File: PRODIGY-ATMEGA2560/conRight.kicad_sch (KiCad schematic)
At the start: 1 part, among them J2 DF40C-100DS-0.4V(51)

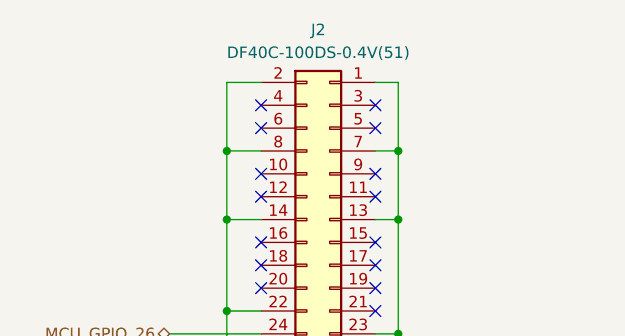
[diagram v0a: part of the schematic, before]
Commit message: ESP32 and ATMEGA bom done.
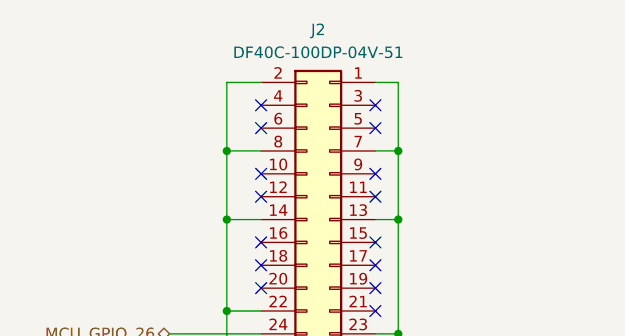
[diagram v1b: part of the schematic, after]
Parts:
- J2: value DF40C-100DS-0.4V(51) -> DF40C-100DP-04V-51; TME (none) -> DF40C-100DP-04V-51
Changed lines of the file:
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@@
 			)
 		)
-		(property "Value" "DF40C-100DS-0.4V(51)"
+		(property "Value" "DF40C-100DP-04V-51 "
 			(at 142.24 32.258 0)
 			(effects
@@
 			(effects
 				(font
+					(size 1.27 1.27)
+				)
+				(hide yes)
+			)
+		)
+		(property "TME" "DF40C-100DP-04V-51 "
+			(at 142.24 31.75 0)
+			(effects
+				(font

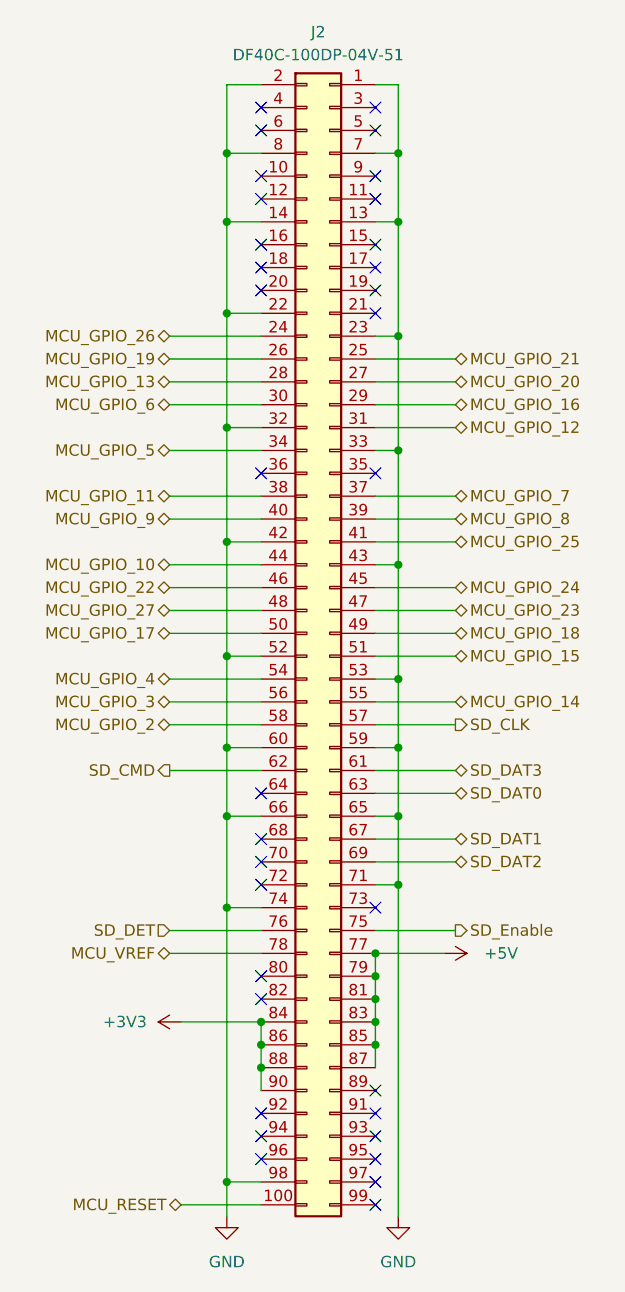
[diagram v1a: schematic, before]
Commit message: Atmega layout done. orientation and alignment testing done. routing started.
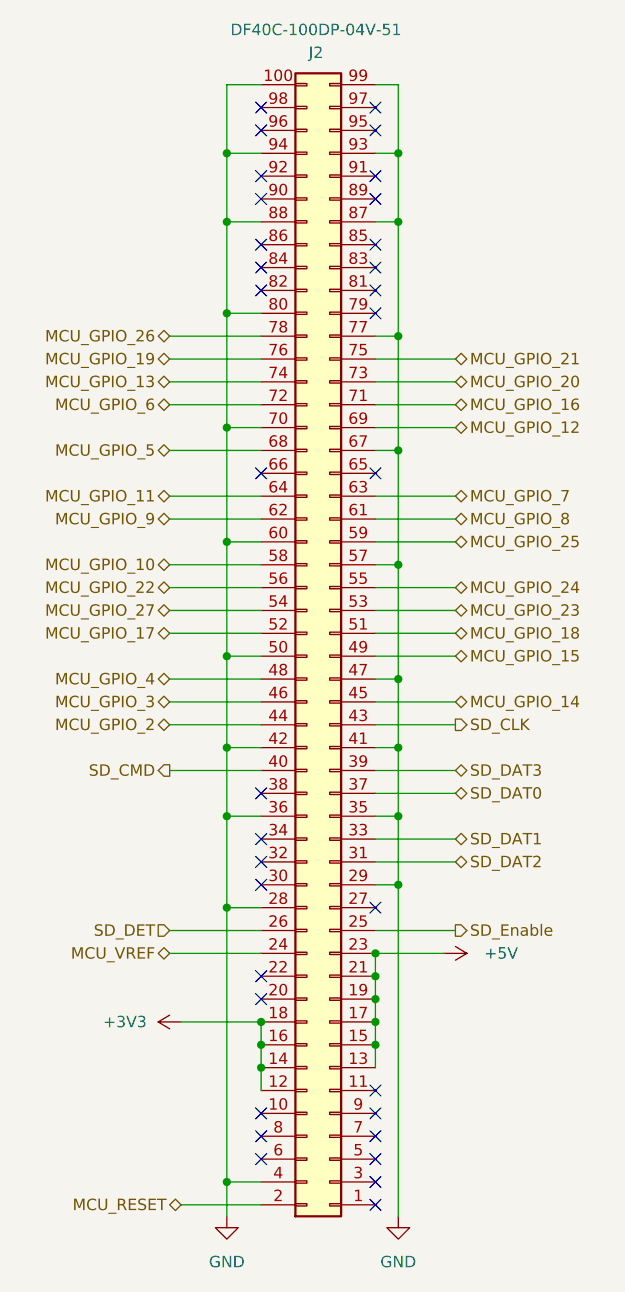
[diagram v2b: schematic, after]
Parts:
- J2: footprint DF40C:HIROSE_DF40C-100DS-0.4V_51_ -> DF40C-100DP-0:DF40C100DP04V51
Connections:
- net +3V3: now also J2.12, J2.14, J2.16, J2.18; no longer J2.84, J2.86, J2.88, J2.90
- net +5V: now also J2.13, J2.15, J2.17, J2.19, J2.21, J2.23; no longer J2.77, J2.79, J2.81, J2.83, J2.85, J2.87
- net GND: now also J2.100, J2.28, J2.29, J2.35, J2.36, J2.4, J2.41, J2.47, J2.50, J2.57, J2.67, J2.70, J2.77, J2.80, J2.87, J2.88, J2.93, J2.94, J2.99; no longer J2.1, J2.13, J2.14, J2.2, J2.22, J2.23, J2.32, J2.33, J2.43, J2.52, J2.53, J2.59, J2.65, J2.66, J2.7, J2.71, J2.74, J2.8, J2.98
- net MCU_GPIO_10: now also J2.58; no longer J2.44
- net MCU_GPIO_11: now also J2.64; no longer J2.38
- net MCU_GPIO_12: now also J2.69; no longer J2.31
- net MCU_GPIO_13: now also J2.74; no longer J2.28
- net MCU_GPIO_14: now also J2.45; no longer J2.55
- net MCU_GPIO_15: now also J2.49; no longer J2.51
- net MCU_GPIO_16: now also J2.71; no longer J2.29
- net MCU_GPIO_17: now also J2.52; no longer J2.50
- net MCU_GPIO_18: now also J2.51; no longer J2.49
- net MCU_GPIO_19: now also J2.76; no longer J2.26
- net MCU_GPIO_2: now also J2.44; no longer J2.58
- net MCU_GPIO_20: now also J2.73; no longer J2.27
- net MCU_GPIO_21: now also J2.75; no longer J2.25
- net MCU_GPIO_22: now also J2.56; no longer J2.46
- net MCU_GPIO_23: now also J2.53; no longer J2.47
- net MCU_GPIO_24: now also J2.55; no longer J2.45
- net MCU_GPIO_25: now also J2.59; no longer J2.41
- net MCU_GPIO_26: now also J2.78; no longer J2.24
- net MCU_GPIO_27: now also J2.54; no longer J2.48
- net MCU_GPIO_3: now also J2.46; no longer J2.56
- net MCU_GPIO_4: now also J2.48; no longer J2.54
- net MCU_GPIO_5: now also J2.68; no longer J2.34
- net MCU_GPIO_6: now also J2.72; no longer J2.30
- net MCU_GPIO_7: now also J2.63; no longer J2.37
- net MCU_GPIO_8: now also J2.61; no longer J2.39
- net MCU_GPIO_9: now also J2.62; no longer J2.40
- net MCU_RESET: now also J2.2; no longer J2.100
- net MCU_VREF: now also J2.24; no longer J2.78
- net SD_CLK: now also J2.43; no longer J2.57
- net SD_CMD: now also J2.40; no longer J2.62
- net SD_DAT0: now also J2.37; no longer J2.63
- net SD_DAT1: now also J2.33; no longer J2.67
- net SD_DAT2: now also J2.31; no longer J2.69
- net SD_DAT3: now also J2.39; no longer J2.61
- net SD_DET: now also J2.26; no longer J2.76
- net SD_Enable: now also J2.25; no longer J2.75
